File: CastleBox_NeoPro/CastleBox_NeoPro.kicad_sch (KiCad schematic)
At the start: 0 parts

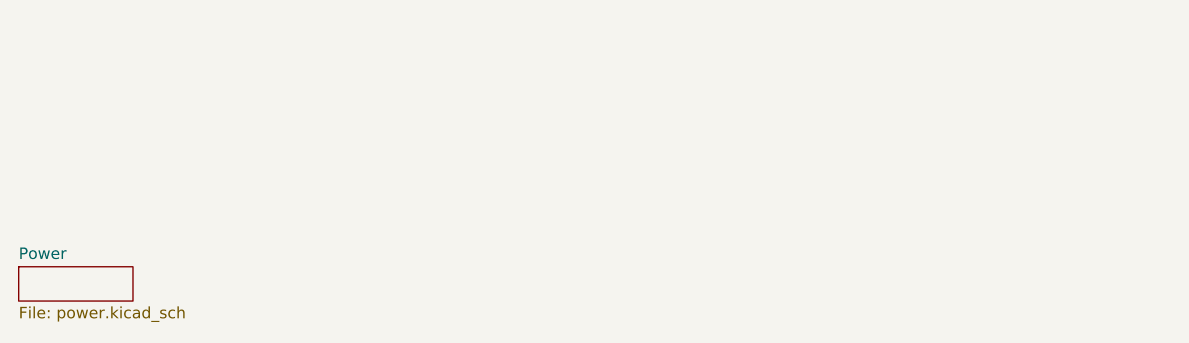
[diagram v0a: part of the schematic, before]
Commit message: added CastleBox NeoPro
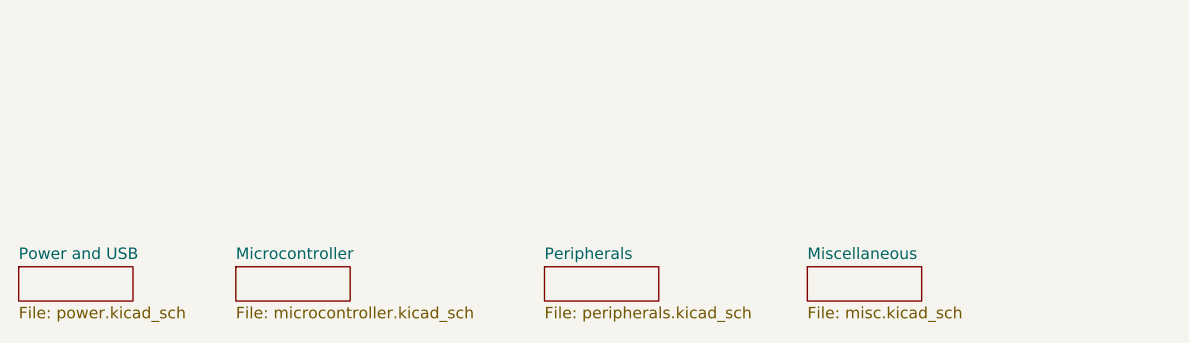
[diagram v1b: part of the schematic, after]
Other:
- sheet Power renamed Power and USB
- added sheet Microcontroller (microcontroller.kicad_sch)
- added sheet Miscellaneous (misc.kicad_sch)
- added sheet Peripherals (peripherals.kicad_sch)
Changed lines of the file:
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@@
+	)
+	(sheet
+		(at 80.01 187.96)
+		(size 12.7 3.81)
+		(exclude_from_sim no)
+		(in_bom yes)
+		(on_board yes)
+		(dnp no)
+		(fields_autoplaced yes)
+		(stroke
+			(width 0.1524)
+			(type solid)
+		)
+		(fill
+			(color 0 0 0 0.0000)
+		)
+		(property "Sheetname" "Peripherals"
+			(at 80.01 187.2484 0)
+			(effects
+				(font
+					(size 1.27 1.27)
+				)
+				(justify left bottom)
+			)
+		)
+		(property "Sheetfile" "peripherals.kicad_sch"
+			(at 80.01 192.3546 0)
+			(effects
+				(font
+					(size 1.27 1.27)
+				)
+				(justify left top)
+			)
+		)
+		(instances
+			(project "CastleBox_NeoPro"
+				(path "/7a7ced68-0c18-429c-b5d2-fe4ce8afef91"
+					(page "4")
+				)
+			)
+		)
+	)
+	(sheet
+		(at 45.72 187.96)
+		(size 12.7 3.81)
+		(exclude_from_sim no)
+		(in_bom yes)
+		(on_board yes)
+		(dnp no)
+		(fields_autoplaced yes)
+		(stroke
+			(width 0.1524)
+			(type solid)
+		)
+		(fill
+			(color 0 0 0 0.0000)
+		)
+		(property "Sheetname" "Microcontroller"
+			(at 45.72 187.2484 0)
+			(effects
+				(font
+					(size 1.27 1.27)
+				)
+				(justify left bottom)
+			)
+		)
+		(property "Sheetfile" "microcontroller.kicad_sch"
+			(at 45.72 192.3546 0)
+			(effects
+				(font
+					(size 1.27 1.27)
+				)
+				(justify left top)
+			)
+		)
+		(instances
+			(project "CastleBox_NeoPro"
+				(path "/7a7ced68-0c18-429c-b5d2-fe4ce8afef91"
+					(page "3")
+				)
+			)
+		)
+	)
+	(sheet
+		(at 109.22 187.96)
+		(size 12.7 3.81)
+		(exclude_from_sim no)
+		(in_bom yes)
+		(on_board yes)
+		(dnp no)
+		(fields_autoplaced yes)
+		(stroke
+			(width 0.1524)
+			(type solid)
+		)
+		(fill
+			(color 0 0 0 0.0000)
+		)
+		(property "Sheetname" "Miscellaneous"
+			(at 109.22 187.2484 0)
+			(effects
+				(font
+					(size 1.27 1.27)
+				)
+				(justify left bottom)
+			)
+		)
+		(property "Sheetfile" "misc.kicad_sch"
+			(at 109.22 192.3546 0)
+			(effects
+				(font
+					(size 1.27 1.27)
+				)
+				(justify left top)
+			)
+		)
+		(instances
+			(project "CastleBox_NeoPro"
+				(path "/7a7ced68-0c18-429c-b5d2-fe4ce8afef91"
+					(page "5")
+				)
+			)
+		)
 	)
 	(sheet
@@
 			(color 0 0 0 0.0000)
 		)
-		(property "Sheetname" "Power"
+		(property "Sheetname" "Power and USB"
 			(at 21.59 187.2484 0)
 			(effects
